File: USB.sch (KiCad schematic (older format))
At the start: 4 parts

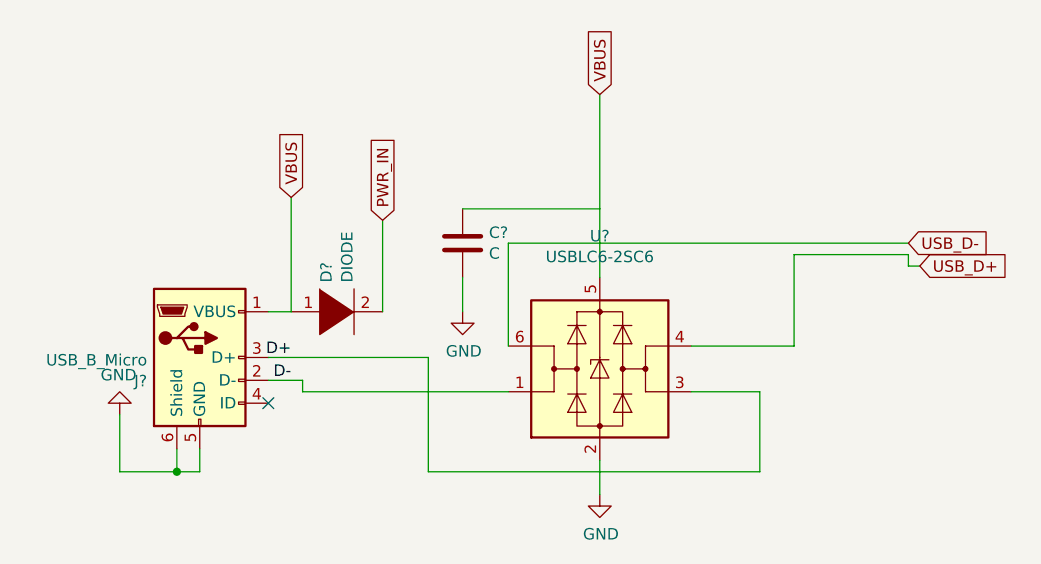
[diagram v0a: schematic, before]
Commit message: 4 layer add
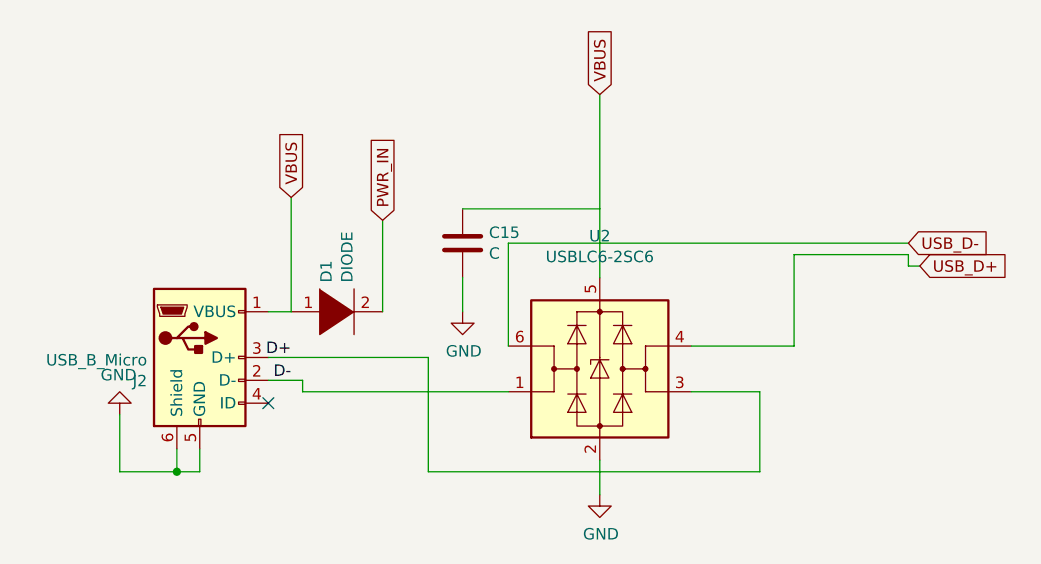
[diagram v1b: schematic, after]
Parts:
- gave numbers to parts that had none: 4
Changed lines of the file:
@@
 $Descr A4 11693 8268
 encoding utf-8
-Sheet 10 10
+Sheet 3 11
 Title ""
 Date ""
@@
 AR Path="/5F5427BF" Ref="U?"  Part="1"
 AR Path="/5F2F6324/5F5427BF" Ref="U?"  Part="1"
-AR Path="/5F53A524/5F5427BF" Ref="U?"  Part="1"
+AR Path="/5F53A524/5F5427BF" Ref="U2"  Part="1"
 AR Path="/5F584BC5/5F5427BF" Ref="U?"  Part="1"
-F 0 "U?" H 5850 4381 50  0000 C CNN
+AR Path="/5FD47887/5F5427BF" Ref="U?"  Part="1"
+F 0 "U2" H 5850 4381 50  0000 C CNN
 F 1 "USBLC6-2SC6" H 5850 4290 50  0000 C CNN
 F 2 "Package_TO_SOT_SMD:SOT-23-6" H 5850 3300 50  0001 C CNN
@@
 AR Path="/5F2F6324/5F5427C8" Ref="#PWR?"  Part="1"
 AR Path="/5F5427C8" Ref="#PWR?"  Part="1"
-AR Path="/5F53A524/5F5427C8" Ref="#PWR?"  Part="1"
+AR Path="/5F53A524/5F5427C8" Ref="#PWR0111"  Part="1"
 AR Path="/5F584BC5/5F5427C8" Ref="#PWR?"  Part="1"
-F 0 "#PWR?" H 3750 3750 50  0001 C CNN
+AR Path="/5FD47887/5F5427C8" Ref="#PWR?"  Part="1"
+F 0 "#PWR0111" H 3750 3750 50  0001 C CNN
 F 1 "GND" H 3755 3827 50  0000 C CNN
 F 2 "" H 3750 4000 50  0001 C CNN
@@
 AR Path="/5F2F6324/5F5427E0" Ref="#PWR?"  Part="1"
 AR Path="/5F5427E0" Ref="#PWR?"  Part="1"
-AR Path="/5F53A524/5F5427E0" Ref="#PWR?"  Part="1"
+AR Path="/5F53A524/5F5427E0" Ref="#PWR0112"  Part="1"
 AR Path="/5F584BC5/5F5427E0" Ref="#PWR?"  Part="1"
-F 0 "#PWR?" H 5850 4100 50  0001 C CNN
+AR Path="/5FD47887/5F5427E0" Ref="#PWR?"  Part="1"
+F 0 "#PWR0112" H 5850 4100 50  0001 C CNN
 F 1 "GND" H 5855 4177 50  0000 C CNN
 F 2 "" H 5850 4350 50  0001 C CNN
@@
 AR Path="/5F2F6324/5F5427E8" Ref="C?"  Part="1"
 AR Path="/5F5427E8" Ref="C?"  Part="1"
-AR Path="/5F53A524/5F5427E8" Ref="C?"  Part="1"
+AR Path="/5F53A524/5F5427E8" Ref="C15"  Part="1"
 AR Path="/5F584BC5/5F5427E8" Ref="C?"  Part="1"
-F 0 "C?" H 5365 3296 50  0000 L CNN
+AR Path="/5FD47887/5F5427E8" Ref="C?"  Part="1"
+F 0 "C15" H 5365 3296 50  0000 L CNN
 F 1 "C" H 5365 3205 50  0000 L CNN
 F 2 "" H 5288 3100 50  0001 C CNN
@@
 AR Path="/5F2F6324/5F5427F0" Ref="#PWR?"  Part="1"
 AR Path="/5F5427F0" Ref="#PWR?"  Part="1"
-AR Path="/5F53A524/5F5427F0" Ref="#PWR?"  Part="1"
+AR Path="/5F53A524/5F5427F0" Ref="#PWR0113"  Part="1"
 AR Path="/5F584BC5/5F5427F0" Ref="#PWR?"  Part="1"
-F 0 "#PWR?" H 5250 3300 50  0001 C CNN
+AR Path="/5FD47887/5F5427F0" Ref="#PWR?"  Part="1"
+F 0 "#PWR0113" H 5250 3300 50  0001 C CNN
 F 1 "GND" H 5255 3377 50  0000 C CNN
 F 2 "" H 5250 3550 50  0001 C CNN
@@
 AR Path="/5F569749/5F5427F7" Ref="D?"  Part="1"
 AR Path="/5F2F6324/5F5427F7" Ref="D?"  Part="1"
-AR Path="/5F53A524/5F5427F7" Ref="D?"  Part="1"
+AR Path="/5F53A524/5F5427F7" Ref="D1"  Part="1"
 AR Path="/5F584BC5/5F5427F7" Ref="D?"  Part="1"
-F 0 "D?" V 4654 3678 50  0000 L CNN
+AR Path="/5FD47887/5F5427F7" Ref="D?"  Part="1"
+F 0 "D1" V 4654 3678 50  0000 L CNN
 F 1 "DIODE" V 4745 3678 50  0000 L CNN
 F 2 "Diode_SMD:D_1206_3216Metric" H 4700 3550 50  0001 C CNN
@@
 AR Path="/5F2F6324/5F5427FF" Ref="J?"  Part="1"
 AR Path="/5F5427FF" Ref="J?"  Part="1"
-AR Path="/5F53A524/5F5427FF" Ref="J?"  Part="1"
+AR Path="/5F53A524/5F5427FF" Ref="J2"  Part="1"
 AR Path="/5F584BC5/5F5427FF" Ref="J?"  Part="1"
-F 0 "J?" H 3870 3647 50  0000 R CNN
+AR Path="/5FD47887/5F5427FF" Ref="J?"  Part="1"
+F 0 "J2" H 3870 3647 50  0000 R CNN
 F 1 "USB_B_Micro" H 3870 3738 50  0000 R CNN
 F 2 "Connector_USB:USB_Micro-B_Molex-105017-0001" H 4250 3700 50  0001 C CNN

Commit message: a
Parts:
- C15: footprint (none) -> Capacitor_SMD:C_0603_1608Metric
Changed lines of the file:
@@
 F 0 "C15" H 5365 3296 50  0000 L CNN
 F 1 "C" H 5365 3205 50  0000 L CNN
-F 2 "" H 5288 3100 50  0001 C CNN
+F 2 "Capacitor_SMD:C_0603_1608Metric" H 5288 3100 50  0001 C CNN
 F 3 "~" H 5250 3250 50  0001 C CNN
 	1    5250 3250

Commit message: finish board
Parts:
- removed C15: C, Capacitor_SMD:C_0603_1608Metric, symbol Device:C
- removed U2: USBLC6-2SC6, Package_TO_SOT_SMD:SOT-23-6, symbol Power_Protection:USBLC6-2SC6
- added R3, R4: 22R, Resistor_SMD:R_0603_1608Metric_Pad1.05x0.95mm_HandSolder, symbol Device:R
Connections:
- net D+: now also R3.1
- net D-: now also R4.1
- net USB_D+: now also R3.2
- net USB_D-: now also R4.2
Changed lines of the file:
@@
 Comment4 ""
 $EndDescr
-$Comp
-L Power_Protection:USBLC6-2SC6 U?
-U 1 1 5F5427BF
-P 5850 3800
-AR Path="/5F5427BF" Ref="U?"  Part="1"
-AR Path="/5F2F6324/5F5427BF" Ref="U?"  Part="1"
-AR Path="/5F53A524/5F5427BF" Ref="U2"  Part="1"
-AR Path="/5F584BC5/5F5427BF" Ref="U?"  Part="1"
-AR Path="/5FD47887/5F5427BF" Ref="U?"  Part="1"
-F 0 "U2" H 5850 4381 50  0000 C CNN
-F 1 "USBLC6-2SC6" H 5850 4290 50  0000 C CNN
-F 2 "Package_TO_SOT_SMD:SOT-23-6" H 5850 3300 50  0001 C CNN
-F 3 "https://www.st.com/resource/en/datasheet/usblc6-2.pdf" H 6050 4150 50  0001 C CNN
-	1    5850 3800
-	1    0    0    -1
-$EndComp
 Wire Wire Line
 	4100 4150 4100 4250
@@
 $EndComp
 NoConn ~ 4400 3950
-Wire Wire Line
-	4550 3850 4550 3900
-Wire Wire Line
-	4550 3850 4400 3850
 Text Label 4500 3750 2    50   ~ 0
 D+
@@
 D-
 Wire Wire Line
-	4550 3900 5450 3900
-Wire Wire Line
-	5100 3750 5100 4250
-Wire Wire Line
-	5100 4250 6550 4250
-Wire Wire Line
-	6550 4250 6550 3900
-Wire Wire Line
-	6550 3900 6250 3900
-Wire Wire Line
 	4400 3750 5100 3750
-Wire Wire Line
-	6250 3700 6700 3700
-Wire Wire Line
-	6700 3700 6700 3300
-Wire Wire Line
-	6700 3300 7200 3300
-Wire Wire Line
-	5450 3700 5450 3250
-Wire Wire Line
-	5450 3250 7200 3250
-Wire Wire Line
-	5850 3400 5850 3100
-Wire Wire Line
-	5850 4200 5850 4350
-$Comp
-L power:GND #PWR?
-U 1 1 5F5427E0
-P 5850 4350
-AR Path="/5F2F6324/5F5427E0" Ref="#PWR?"  Part="1"
-AR Path="/5F5427E0" Ref="#PWR?"  Part="1"
-AR Path="/5F53A524/5F5427E0" Ref="#PWR0112"  Part="1"
-AR Path="/5F584BC5/5F5427E0" Ref="#PWR?"  Part="1"
-AR Path="/5FD47887/5F5427E0" Ref="#PWR?"  Part="1"
-F 0 "#PWR0112" H 5850 4100 50  0001 C CNN
-F 1 "GND" H 5855 4177 50  0000 C CNN
-F 2 "" H 5850 4350 50  0001 C CNN
-F 3 "" H 5850 4350 50  0001 C CNN
-	1    5850 4350
-	1    0    0    -1
-$EndComp
-Wire Wire Line
-	7250 3350 7200 3350
-Wire Wire Line
-	7200 3350 7200 3300
-$Comp
-L Device:C C?
-U 1 1 5F5427E8
-P 5250 3250
-AR Path="/5F2F6324/5F5427E8" Ref="C?"  Part="1"
-AR Path="/5F5427E8" Ref="C?"  Part="1"
-AR Path="/5F53A524/5F5427E8" Ref="C15"  Part="1"
-AR Path="/5F584BC5/5F5427E8" Ref="C?"  Part="1"
-AR Path="/5FD47887/5F5427E8" Ref="C?"  Part="1"
-F 0 "C15" H 5365 3296 50  0000 L CNN
-F 1 "C" H 5365 3205 50  0000 L CNN
-F 2 "Capacitor_SMD:C_0603_1608Metric" H 5288 3100 50  0001 C CNN
-F 3 "~" H 5250 3250 50  0001 C CNN
-	1    5250 3250
-	1    0    0    -1
-$EndComp
-Wire Wire Line
-	5250 3100 5850 3100
-Wire Wire Line
-	5250 3400 5250 3550
-$Comp
-L power:GND #PWR?
-U 1 1 5F5427F0
-P 5250 3550
-AR Path="/5F2F6324/5F5427F0" Ref="#PWR?"  Part="1"
-AR Path="/5F5427F0" Ref="#PWR?"  Part="1"
-AR Path="/5F53A524/5F5427F0" Ref="#PWR0113"  Part="1"
-AR Path="/5F584BC5/5F5427F0" Ref="#PWR?"  Part="1"
-AR Path="/5FD47887/5F5427F0" Ref="#PWR?"  Part="1"
-F 0 "#PWR0113" H 5250 3300 50  0001 C CNN
-F 1 "GND" H 5255 3377 50  0000 C CNN
-F 2 "" H 5250 3550 50  0001 C CNN
-F 3 "" H 5250 3550 50  0001 C CNN
-	1    5250 3550
-	1    0    0    -1
-$EndComp
 Wire Wire Line
 	4400 3550 4500 3550
@@
 	1    0    0    -1
 $EndComp
-Text GLabel 7200 3250 2    50   Input ~ 0
+Text GLabel 5600 3850 2    50   Input ~ 0
 USB_D-
-Text GLabel 7250 3350 2    50   Input ~ 0
+Text GLabel 5600 3750 2    50   Input ~ 0
 USB_D+
 $Comp
@@
 Text GLabel 4500 3050 1    50   Input ~ 0
 VBUS
+$Comp
+L Device:R R?
+U 1 1 5F59BCFB
+P 5250 3750
+AR Path="/5F41B667/5F59BCFB" Ref="R?"  Part="1"
+AR Path="/5F59BCFB" Ref="R?"  Part="1"
+AR Path="/5F5517E4/5F59BCFB" Ref="R?"  Part="1"
+AR Path="/5F5C31DE/5F59BCFB" Ref="R?"  Part="1"
+AR Path="/5F53A524/5F59BCFB" Ref="R3"  Part="1"
+F 0 "R3" H 5320 3796 50  0000 L CNN
+F 1 "22R" H 5320 3705 50  0000 L CNN
+F 2 "Resistor_SMD:R_0603_1608Metric_Pad1.05x0.95mm_HandSolder" V 5180 3750 50  0001 C CNN
+F 3 "~" H 5250 3750 50  0001 C CNN
+	1    5250 3750
+	0    -1   -1   0
+$EndComp
+$Comp
+L Device:R R?
+U 1 1 5F59BEBC
+P 5250 3850
+AR Path="/5F41B667/5F59BEBC" Ref="R?"  Part="1"
+AR Path="/5F59BEBC" Ref="R?"  Part="1"
+AR Path="/5F5517E4/5F59BEBC" Ref="R?"  Part="1"
+AR Path="/5F5C31DE/5F59BEBC" Ref="R?"  Part="1"
+AR Path="/5F53A524/5F59BEBC" Ref="R4"  Part="1"
+F 0 "R4" H 5320 3896 50  0000 L CNN
+F 1 "22R" H 5320 3805 50  0000 L CNN
+F 2 "Resistor_SMD:R_0603_1608Metric_Pad1.05x0.95mm_HandSolder" V 5180 3850 50  0001 C CNN
+F 3 "~" H 5250 3850 50  0001 C CNN
+	1    5250 3850
+	0    -1   -1   0
+$EndComp
 Wire Wire Line
-	5850 2600 5850 3100
-Text GLabel 5850 2600 1    50   Input ~ 0
-VBUS
+	4400 3850 5100 3850
+Wire Wire Line
+	5400 3750 5600 3750
+Wire Wire Line
+	5400 3850 5600 3850
 $EndSCHEMATC
